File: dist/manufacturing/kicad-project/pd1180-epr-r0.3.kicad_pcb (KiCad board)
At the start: 4 copper layers, 85.9 x 85.9 mm, 266 parts, among them J1 J1, J2 J2, J3 J3, J6 J6, J7 J7, J9 J9, Q1 Q1, Q10 Q10, Q11 Q11, Q12 Q12, Q13 Q13, Q14 Q14, Q15 Q15, Q16 Q16, Q17 Q17, Q18 Q18, Q19 Q19, Q2 Q2, Q20 Q20, Q21 Q21, Q22 Q22, Q23 Q23, Q24 Q24, Q25 Q25, Q3 Q3, Q4 Q4, Q5 Q5, Q6 Q6, Q7 Q7, Q8 Q8, Q9 Q9, SW1 SW1, U1 TPD4S480RUKR, U10 SN74LVC1G08DBVR, U11 SN74LVC1G08DBVR, U12 TL431AIDBZR, U13 TLV3201AIDBVR, U14 TLV3201AIDBVR, U15 UCC27511DBVR, U16 STM32G0B1CBT6, U17 W25Q32JVSSIQ, U18 AS5047P-ATSM, U19 TCAN332DR, U2 TPS26750SRSMR, U20 MAX3485EESA+T, U21 MAX3232ESE+T, U22 LMR36510ADDAR, U23 LM66100DCKR, U24 LM66100DCKR, U3 M24512-RMN6TP, U4 SN74LVC1G08DBVR, U5 LMR36510ADDAR, U6 TPS26631RGER, U7 TMC5160A-TA-T, U8 74LVC1G157GW,125, U9 74LVC1G157GW,125, Y1 Y1

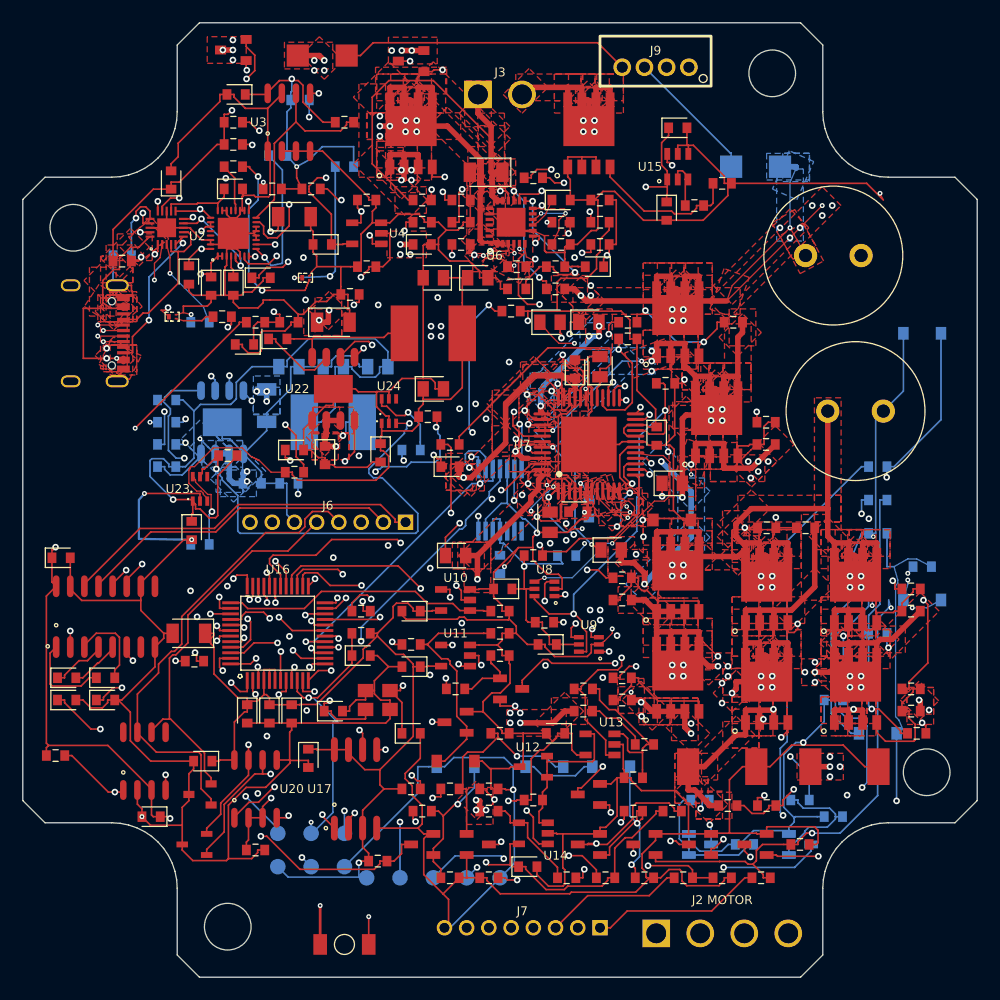
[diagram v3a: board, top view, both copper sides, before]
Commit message: Implement dual USB power/data ECO and consolidate industrial I/O
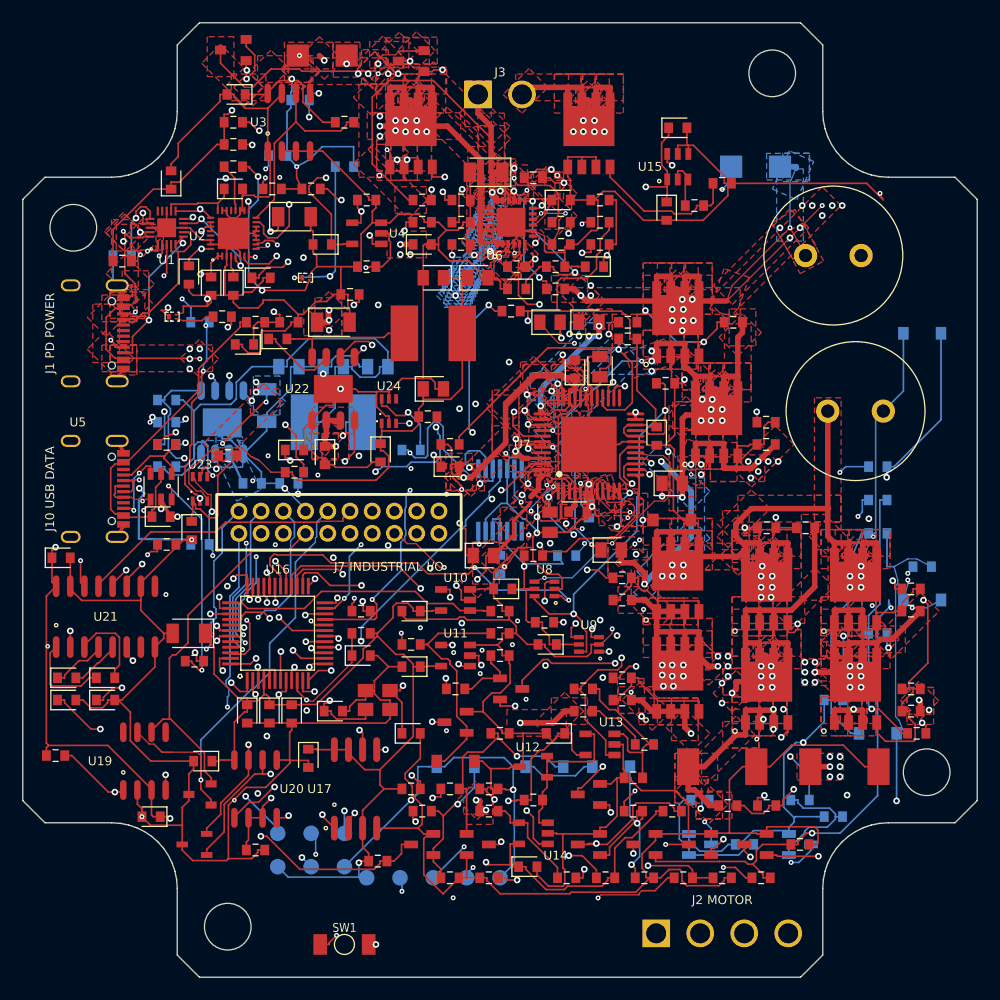
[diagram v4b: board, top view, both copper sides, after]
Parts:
- removed J6: J6, B8B-PH-K-S_LF_SN
- removed J9: J9, B4B-PH-K-S_LF_SN
- added C73: 100nF, capacitor_cap0603, F.Cu at (69.5, 101.5)
- added D15: USBLC6-4SC6, USBLC6-4SC6, F.Cu at (69.5, 98.8)
- added J10: J10, USB4105-GF-A, F.Cu at (63.6, 99.0)
- added R105: 5.1kΩ, resistor_res0603, F.Cu at (70.0, 95.0)
- added R106: 5.1kΩ, resistor_res0603, F.Cu at (70.0, 104.0)
- J7: value J7 -> B20B-PHDSS(LF)(SN); footprint B8B-PH-K-S_LF_SN -> B20B-PHDSS_LF_SN
- Q10: value Q10 -> CSD19534Q5A
- Q11: value Q11 -> CSD19534Q5A
- Q12: value Q12 -> CSD19534Q5A
- Q13: value Q13 -> CSD19534Q5A
- Q16: value Q16 -> CSD19534Q5A
- Q2: value Q2 -> CSD17484F4
- Q3: value Q3 -> CSD17484F4
- Q4: value Q4 -> CSD19534Q5A
- Q6: value Q6 -> CSD19534Q5A
- Q7: value Q7 -> CSD19534Q5A
- Q8: value Q8 -> CSD19534Q5A
- Q9: value Q9 -> CSD19534Q5A
- moved J7 40.1 mm to (85.5, 102.0)
- moved C34 2.50 mm to (98.5, 105.0)
- turned D12 to 180 degrees
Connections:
- net V3V3_USB renamed V3V3_PD
- C11 pad 1: USB_VBUS -> PD_VBUS
- C12 pad 1: USB_VBUS -> PD_VBUS
- J1 pad 10: unconnected-(J1-SBU1-Pad10) -> PD_SBU1_CONN
- J1 pad 11: USB_DP_CONN -> unconnected-(J1-DP2-Pad11)
- J1 pad 12: USB_DM_CONN -> unconnected-(J1-DM-Pad12)
- J1 pad 13: USB_DP_CONN -> unconnected-(J1-DP-Pad13)
- J1 pad 14: USB_DM_CONN -> unconnected-(J1-DN2-Pad14)
- J1 pad 16: unconnected-(J1-SBU2-Pad16) -> PD_SBU2_CONN
- J1 pad 17: USB_VBUS -> PD_VBUS
- J1 pad 18: USB_VBUS -> PD_VBUS
- J1 pad 7: USB_VBUS -> PD_VBUS
- J1 pad 8: USB_VBUS -> PD_VBUS
- Q1 pad 3: USB_VBUS -> PD_VBUS
- Q4 pad 1: USB_VBUS -> PD_VBUS
- Q4 pad 2: USB_VBUS -> PD_VBUS
- Q4 pad 3: USB_VBUS -> PD_VBUS
- Q5 pad 2: USB_VBUS -> PD_VBUS
- R107 pad 1: USB_VBUS -> USB_DATA_VBUS
- R19 pad 1: USB_VBUS -> PD_VBUS
- R22 pad 1: USB_VBUS -> PD_VBUS
- R71 pad 1: USB_DP_PROTECTED -> USB_DP_CONN
- R72 pad 1: USB_DM_PROTECTED -> USB_DM_CONN
- U1 pad 1: USB_DP_CONN -> PD_SBU1_CONN
- U1 pad 14: USB_DM_PROTECTED -> unconnected-(U1-SBU2-Pad14)
- U1 pad 15: USB_DP_PROTECTED -> unconnected-(U1-SBU1-Pad15)
- U1 pad 2: USB_DM_CONN -> PD_SBU2_CONN
- U1 pad 20: USB_VBUS -> PD_VBUS
- U5 pad 2: USB_VBUS -> PD_VBUS
- U5 pad 3: USB_VBUS -> PD_VBUS
- U6 pad 5: USB_VBUS -> PD_VBUS
- U7 pad 23: ENC_B -> GND
- U7 pad 24: ENC_A -> GND
- U7 pad 25: ENC_I -> unconnected-(U7-ENCN_DCO_CFG6-Pad25)
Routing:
- net USB_VBUS: track 151.3 -> 0.00 mm, vias 29 -> 0
- net PD_VBUS: track 0.00 -> 146.5 mm, vias 0 -> 23
- net USB_DP_PROTECTED: track 56.9 -> 0.00 mm, vias 3 -> 0
- net HOME_24V: track 15.5 -> 70.7 mm, vias 0 -> 2
- net USB_DM_PROTECTED: track 46.4 -> 0.00 mm, vias 3 -> 0
- net OUT0: track 84.9 -> 127.1 mm, vias 1 -> 3
- net STOPR_24V: track 12.5 -> 54.3 mm, vias 0 -> 2
- net HW_ENABLE_24V: track 67.2 -> 28.6 mm, vias 1 -> 2
- net STOPL_24V: track 12.2 -> 45.2 mm, vias 1 -> 2
- net USB_DATA_VBUS: track 0.00 -> 31.5 mm
- net ENC_I: track 62.2 -> 34.8 mm
- net ENC_B: track 65.5 -> 45.1 mm
- net DIN0_24V: track 15.6 -> 35.6 mm, vias 1 -> 2
- net OUT1: track 111.3 -> 130.0 mm, vias 1 -> 4
- net DIR_24V: track 68.2 -> 52.8 mm, vias 1 -> 2
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- added copper zone on B.Cu, net BRAKE_RETURN
- added copper zone on B.Cu, net EFUSE_IN
- added copper zone on B.Cu, net MOTOR_B1
- added copper zone on B.Cu, net PD_VBUS
- added copper zone on F.Cu, net PD_VBUS
- added copper zone on In1.Cu, net PD_VBUS
- added copper zone on In2.Cu, net PD_VBUS
- removed copper zone on B.Cu, net USB_VBUS
- removed copper zone on F.Cu, net USB_VBUS
- removed copper zone on In1.Cu, net USB_VBUS
- removed copper zone on In2.Cu, net USB_VBUS
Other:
- board text added: "J1 PD POWER"
- board text added: "J10 USB DATA"
- board text added: "J7 INDUSTRIAL I/O"
- board text added: "SW1"
- board text added: "Stepper Controller with USB-C PD 3.1 EPR · r0.4 ECO"
- board text added: "U1"
- board text added: "U19"
- board text added: "U21"
- board text added: "U5"
- board text added: "ts"
- board text removed: "J6"
- board text removed: "J7"
- board text removed: "J9"
- board text removed: "Stepper Controller with USB-C PD 3.1 EPR · r0.3"
